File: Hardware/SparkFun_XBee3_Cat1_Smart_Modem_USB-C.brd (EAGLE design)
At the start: 35.6 x 59.7 mm, 106 parts, among them J3 USB Female Type C Connector, J4 QWIIC_RIGHT_ANGLE, U2 AP63203, U5 ESD Diode, U7 FT231XS

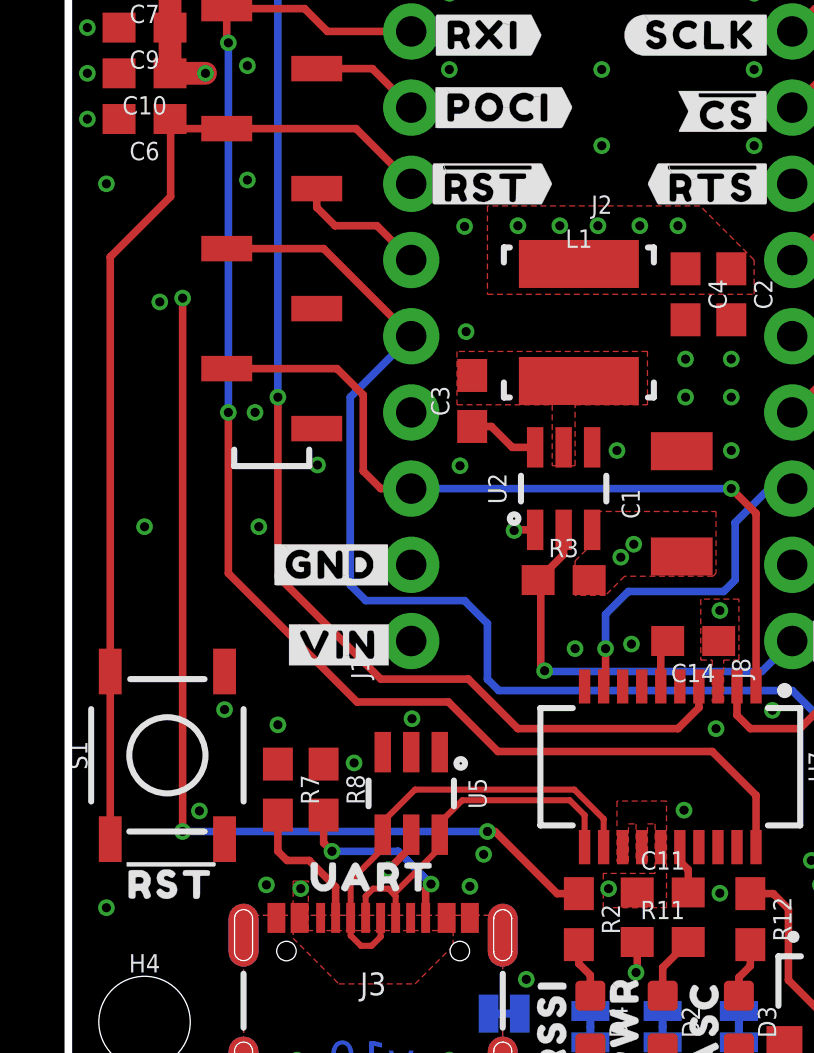
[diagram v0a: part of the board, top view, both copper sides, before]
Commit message: Approves various DRC issues
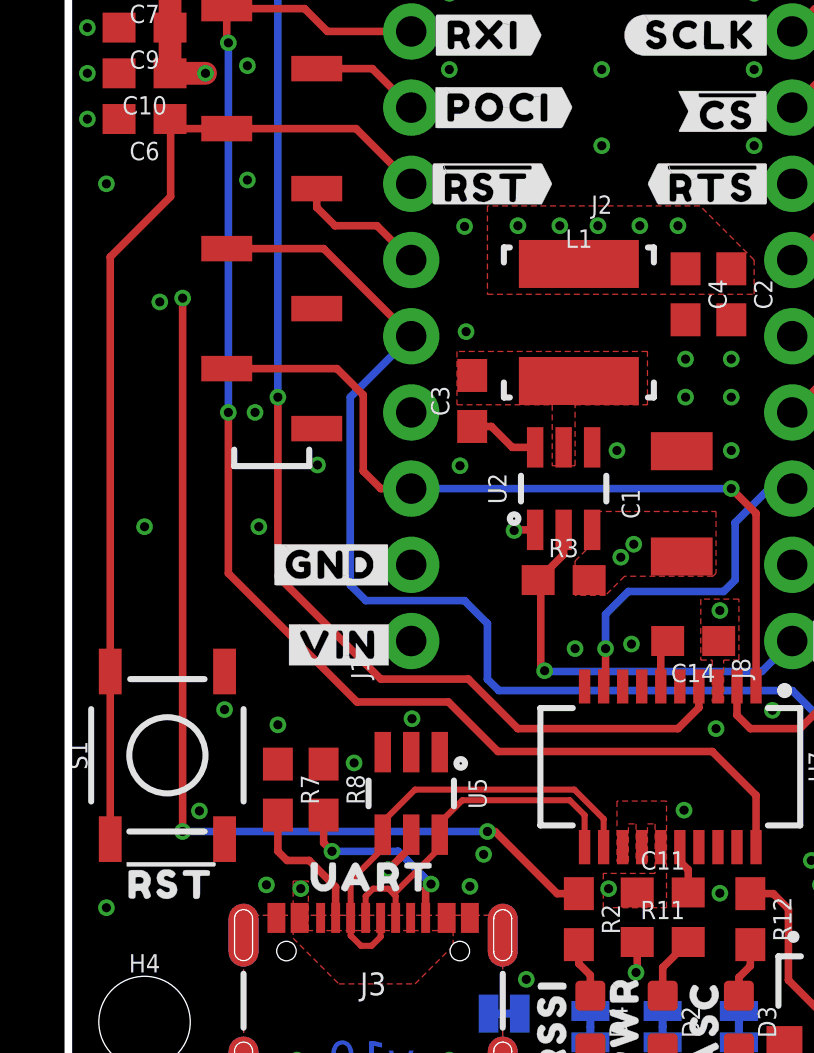
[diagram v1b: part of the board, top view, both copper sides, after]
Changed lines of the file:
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@@
 <element name="D2" library="SparkFun-LED" package="LED-0603" value="Red" x="19.812" y="2.54" smashed="yes" rot="R270">
 <attribute name="NAME" x="20.447" y="2.54" size="0.6096" layer="25" font="vector" ratio="20" rot="R270" align="bottom-center"/>
-<attribute name="PROD_ID" value="DIO-16511" x="19.812" y="2.54" size="1.778" layer="27" rot="R270" display="off"/>
-<attribute name="VALUE" value="Red" x="19.177" y="2.54" size="0.6096" layer="27" font="vector" ratio="20" rot="R270" align="top-center"/>
+<attribute name="PROD_ID" value="DIO-17976" x="19.812" y="2.54" size="1.778" layer="27" rot="R270" display="off"/>
 </element>
 <element name="D3" library="SparkFun-LED" package="LED-0603" value="BLUE" x="22.352" y="2.54" smashed="yes" rot="R270">
@@
 <contactref element="R2" pad="1"/>
 <contactref element="J6" pad="6"/>
-<wire x1="8.28" y1="30.32" x2="8.44" y2="30.48" width="0.254" layer="1"/>
 <wire x1="8.28" y1="30.32" x2="8.28" y2="29.693" width="0.254" layer="1"/>
 <wire x1="10.287" y1="29.083" x2="11.43" y2="27.94" width="0.254" layer="1"/>
@@
 <wire x1="7.747" y1="7.62" x2="7.747" y2="6.985" width="0.762" layer="15"/>
 <via x="7.747" y="6.985" extent="1-16" drill="0.3048"/>
-<wire x1="11.43" y1="8.382" x2="10.668" y2="7.62" width="0.254" layer="1"/>
 <via x="10.668" y="7.62" extent="1-16" drill="0.3048"/>
+<wire x1="11.049" y1="8.001" x2="10.668" y2="7.62" width="0.254" layer="1"/>
 <wire x1="10.668" y1="7.62" x2="7.747" y2="7.62" width="0.254" layer="15"/>
 <via x="18.8468" y="18.4658" extent="1-16" drill="0.3048"/>
@@
 <vertex x="8.001" y="7.239"/>
 </polygon>
-<wire x1="11.43" y1="8.382" x2="11.43" y2="8.7849" width="0" layer="19" extent="1-1"/>
+<wire x1="11.43" y1="8.7849" x2="11.43" y2="8.382" width="0.254" layer="1"/>
+<wire x1="11.43" y1="8.382" x2="11.049" y2="8.001" width="0.254" layer="1"/>
 </signal>
 </signals>
